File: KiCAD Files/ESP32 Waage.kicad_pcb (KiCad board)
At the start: 2 copper layers, 88.8 x 60.3 mm, 25 parts, among them J1 3.3V spare, J10 I2S Terminal, J11 Ext. BME280, J12 Int. BME280, J2 Ext. Power Supply 5V, J3 spare, J4 spare, J5 5V spare, J6 spare, J7 spare, J8 Scale Terminal, J9 DS18B20 Term., SW1 SW_SPST, U1 SN74LVC1T45DBV, U2 ESP32WROVERSocket, U3 HX711Socket

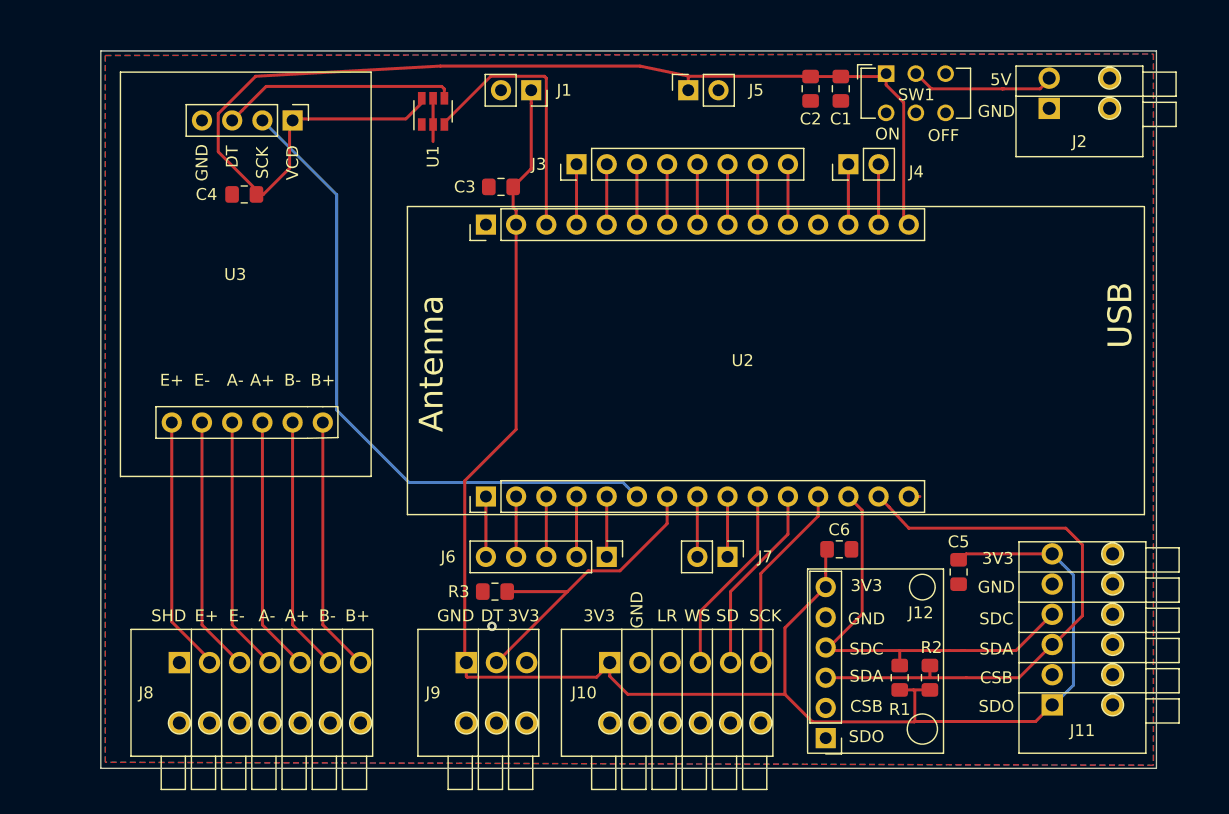
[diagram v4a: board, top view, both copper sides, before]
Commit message: change from 2,54 terminals to 3,81 because of availability removed internal I2C & BME280 added mounting holes
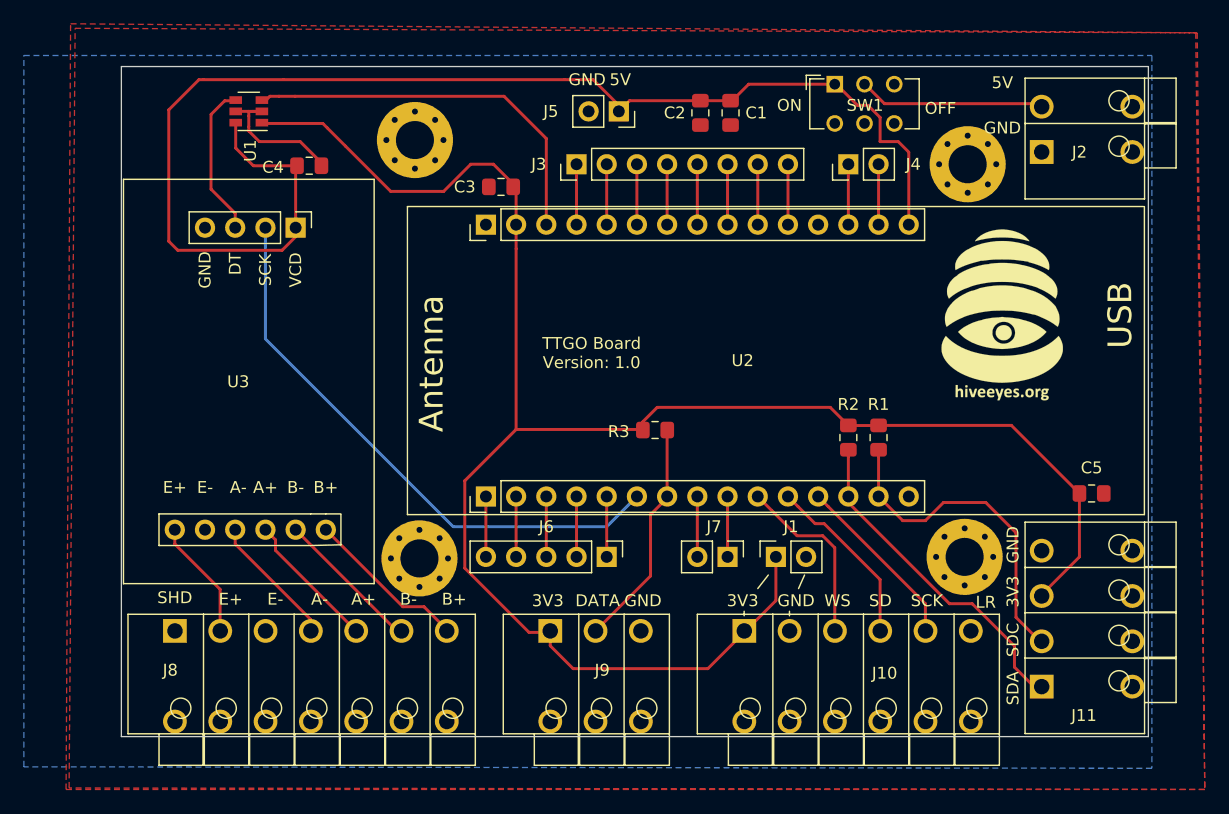
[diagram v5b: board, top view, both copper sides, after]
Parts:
- removed C6: 1uF, Capacitor_SMD:C_0805_2012Metric_Pad1.15x1.40mm_HandSolder
- removed J12: Int. BME280, ESP32 Waage:BME280_Socket
- added  : MountingHole_3.2mm_M3_Pad_Via, MountingHole:MountingHole_3.2mm_M3_Pad_Via, F.Cu at (209.4, 69.2)
- added  : MountingHole_3.2mm_M3_Pad_Via, MountingHole:MountingHole_3.2mm_M3_Pad_Via, F.Cu at (162.9, 67.2)
- added  : MountingHole_3.2mm_M3_Pad_Via, MountingHole:MountingHole_3.2mm_M3_Pad_Via, F.Cu at (163.3, 102.4)
- added  : MountingHole_3.2mm_M3_Pad_Via, MountingHole:MountingHole_3.2mm_M3_Pad_Via, F.Cu at (209.2, 102.2)
- added G***: LOGO, ESP32 Waage:Hiveeyes, F.Cu at (212.3, 81.9)
- J10: footprint ESP32 Waage:PhoenixContact_FFKDSV_254_6_pol -> ESP32 Waage:PhoenixContact_FFKDSV_381_6_pol
- J11: value Ext. BME280 -> I2C Terminal; footprint ESP32 Waage:PhoenixContact_FFKDSV_254_6_pol -> ESP32 Waage:PhoenixContact_FFKDSV_381_4_pol
- J2: footprint ESP32 Waage:PhoenixContact_FFKDSV_254_2_pol -> ESP32 Waage:PhoenixContact_FFKDSV_381_2_pol
- J8: footprint ESP32 Waage:PhoenixContact_FFKDSV_254_7_pol -> ESP32 Waage:PhoenixContact_FFKDSV_381_7_pol
- J9: footprint ESP32 Waage:PhoenixContact_FFKDSV_254_3_pol -> ESP32 Waage:PhoenixContact_FFKDSV_381_3_pol
- moved J1 44.3 mm to (193.3, 102.2), turned to 90 degrees
- moved R2 21.3 mm to (199.4, 92.2), turned to 90 degrees
- moved R1 20.3 mm to (201.9, 92.2), turned to 90 degrees
- moved R3 19.1 mm to (183.1, 91.6), turned to 180 degrees
- moved J10 16.6 mm to (200.7, 107.1)
- moved U1 15.5 mm to (149.0, 64.8), turned to 180 degrees
- moved C5 13.0 mm to (219.8, 96.9), turned to 180 degrees
- moved J9 10.7 mm to (176.7, 107.1)
- moved C2 9.49 mm to (186.9, 64.9)
- moved C1 9.49 mm to (189.5, 64.9)
- moved U3 9.02 mm to (148.8, 74.5)
- moved J8 7.50 mm to (152.8, 107.1)
- moved J5 6.11 mm to (180.1, 64.8), turned to 270 degrees
- moved C4 5.97 mm to (154.1, 69.3), turned to 180 degrees
- moved J11 5.29 mm to (214.2, 110.7)
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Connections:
- C5 pad 1: +3V3 -> GND
- C5 pad 2: GND -> +3V3
- J10 pad 3: GND -> WS
- J10 pad 4: WS -> SD
- J10 pad 5: SD -> SCK
- J10 pad 6: SCK -> GND
- J11 pad 1: +3V3 -> SDA
- J11 pad 2: (no net) -> SDC
- J11 pad 3: SDA -> +3V3
- J11 pad 4: SDC -> GND
- J11 pad 5: GND -> (no net)
- J11 pad 6: +3V3 -> (no net)
- R3 pad 1: GND -> 33
- R3 pad 2: 33 -> +3V3
- U1 pad 1: (no net) -> +3V3
- U2 pad 13: SDC -> SDA
- U2 pad 15: SDA -> SDC
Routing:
- net SDA: track 48.6 -> 27.3 mm
- net GND: track 25.7 -> 11.5 mm, vias 1 -> 0
- net Net-(J8-Pad2): track 21.4 -> 9.96 mm
- net Net-(J8-Pad4): track 21.3 -> 11.1 mm
- net +3V3: track 144.7 -> 154.7 mm
- net +5V: track 99.0 -> 108.7 mm
- net Net-(J8-Pad5): track 21.3 -> 11.7 mm
- net 21: track 22.7 -> 32.0 mm
- net Net-(J8-Pad6): track 21.3 -> 12.4 mm
- net SDC: track 35.5 -> 27.3 mm
- net Net-(J8-Pad7): track 21.3 -> 13.6 mm
- net 32: track 55.5 -> 48.0 mm
- net Net-(U1-Pad4): track 20.0 -> 12.6 mm
- net 33: track 26.4 -> 19.3 mm
- net +5VL: track 12.2 -> 14.8 mm
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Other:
- board size 88.8 x 60.3 mm -> 86.4 x 56.3 mm
- board text added: "DATA"
- board text added: "TTGO Board Version: 1.0"
- board text removed: "CSB"
- board text removed: "DT"
- board text removed: "SDO"
